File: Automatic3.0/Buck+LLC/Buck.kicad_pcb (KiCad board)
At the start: 2 copper layers, 26 parts, among them J1 OUT, J2 LED, J3 LED, J4 Conn_01x11, J5 LM324, J6 J, J7 Conn_01x01, J8 Conn_01x01, Q1 TIP122, Q2 TIP122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

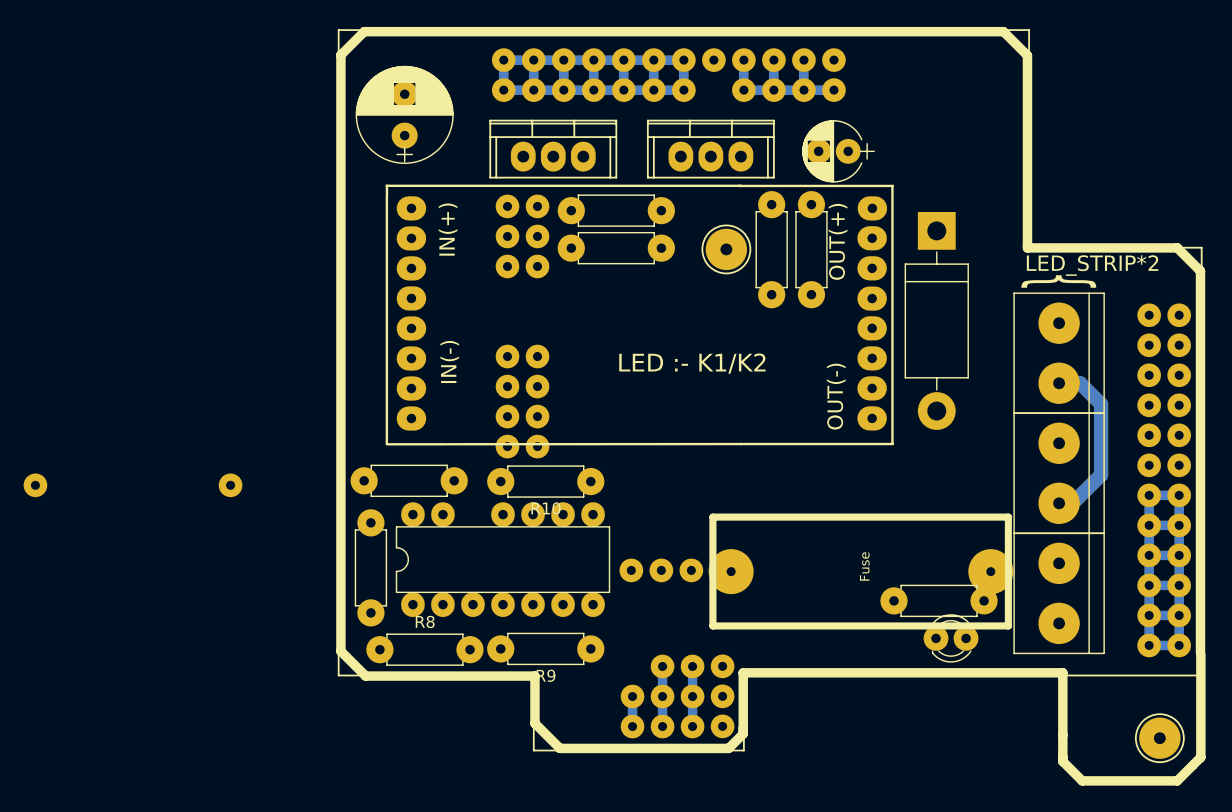
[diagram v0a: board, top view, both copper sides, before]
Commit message: Final automatic base circuits for ABU_ROBOCON_2018 completed
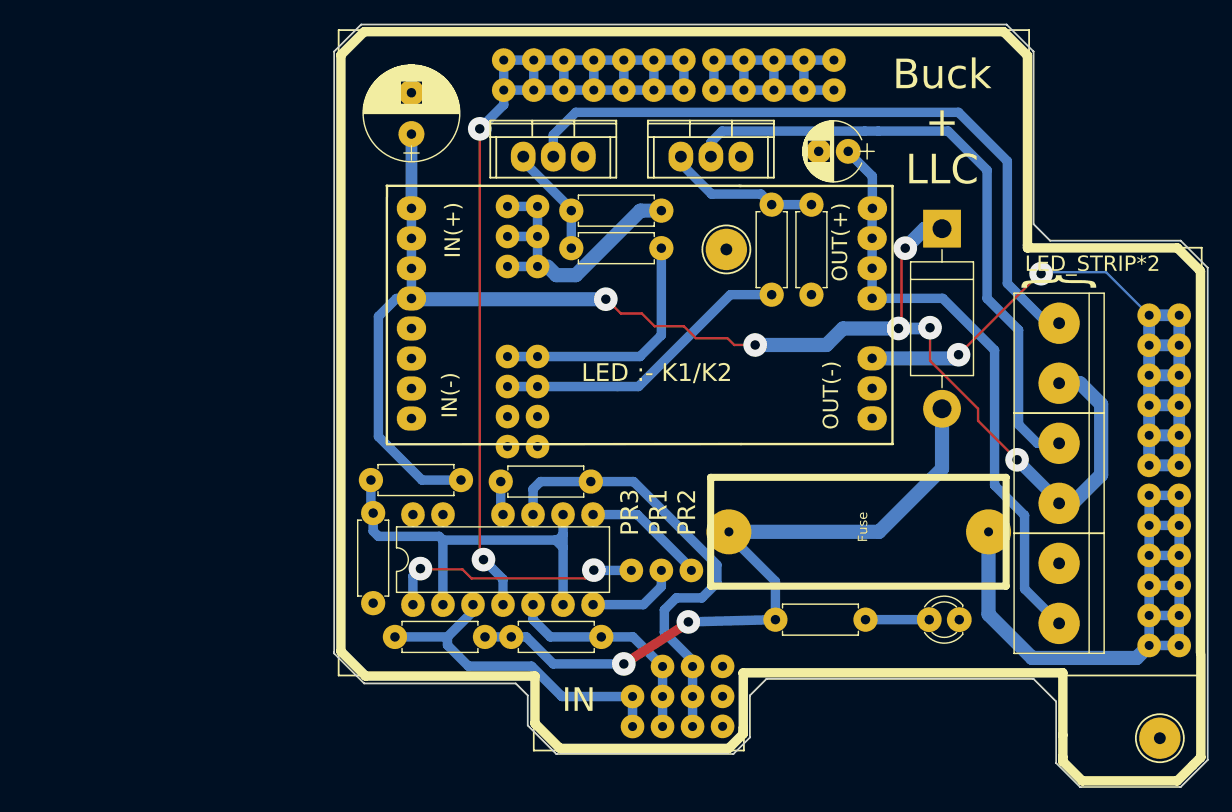
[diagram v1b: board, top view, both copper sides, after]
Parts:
- removed J6: J, modFiles:Jumper
- moved R1 10.2 mm to (214.0, 111.1)
- moved F1 3.37 mm to (213.6, 103.1)
- moved D2 2.53 mm to (221.9, 111.1), turned to 180 degrees
- moved R8 1.67 mm to (174.2, 112.5)
- moved R9 1.35 mm to (191.6, 112.5)
- moved R7 0.85 mm to (172.3, 102.0)
- moved C1 0.59 mm to (175.6, 70.0)
- moved R6 0.58 mm to (172.1, 99.3)
- moved D1 0.48 mm to (220.5, 78.0)
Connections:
- J4 pad 4: /IN1+ -> /IN2+
- J4 pad 5: /IN2+ -> /IN3+
- J4 pad 6: /IN3+ -> /IN1+
- J4 pad 7: /OUT1 -> /OUT2
- J4 pad 8: /OUT2 -> /OUT3
- J4 pad 9: /OUT3 -> /OUT1
- R8 pad 2: +12V -> Net-(D1-Pad2)
- R9 pad 2: +12V -> Net-(D1-Pad2)
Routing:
- net GND: track 15.2 -> 127.7 mm, vias 0 -> 2
- net Net-(C1-Pad1): track 15.9 -> 128.2 mm, vias 0 -> 6
- net Net-(D1-Pad2): track 0.00 -> 61.0 mm, vias 0 -> 2
- net Net-(J2-Pad2): track 0.00 -> 58.9 mm
- net Net-(J3-Pad2): track 0.00 -> 53.1 mm
- net Net-(C2-Pad1): track 0.00 -> 50.8 mm
- net +5V: track 48.3 -> 93.5 mm, vias 0 -> 2
- net /IN3+: track 2.54 -> 38.7 mm
- net /IN1-: track 0.00 -> 35.7 mm
- net /LED2: track 0.00 -> 25.6 mm
- net /IN1+: track 5.08 -> 29.3 mm
- net +12V: track 40.6 -> 63.2 mm
- net /OUT1: track 0.00 -> 21.8 mm, vias 0 -> 2
- net /LED1: track 0.00 -> 21.1 mm
- net /IN2+: track 5.08 -> 19.0 mm
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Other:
- board outline added: 73.9 x 64.5 mm
- net class Default: trace_width 0.25 -> 0.8; via_dia 0.6 -> 2; via_drill 0.4 -> 0.8
- board text added: "Buck + LLC"
- board text added: "IN"
- board text added: "PR3 PR1 PR2"

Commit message: Final for ABU_ROBOCON_2018 Automatic_Base
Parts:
- added J6: LED, modFiles:Connector_Bornier_2, F.Cu at (230.3, 111.4)
- added Q3: TIP122, modFiles:Voltage_Regulators, F.Cu at (224.3, 109.3)
- added R11: 2K2, modFiles:Resistor_small, F.Cu at (216.1, 111.3)
- added R12: 10K, modFiles:Resistor_small, F.Cu at (219.5, 111.3)
- J4: value Conn_01x11 -> Conn_01x12
- moved Q1 38.7 mm to (224.4, 84.0), turned to 90 degrees
- moved J1 36.6 mm to (222.5, 75.6)
- moved Q2 34.3 mm to (224.5, 96.8), turned to 90 degrees
- moved R3 33.6 mm to (219.4, 91.0), turned to 90 degrees
- moved R2 29.3 mm to (216.1, 91.0), turned to 90 degrees
- moved D1 27.9 mm to (192.7, 79.9)
- moved R4 27.1 mm to (216.2, 101.1), turned to 90 degrees
- moved R5 27.1 mm to (219.4, 101.1), turned to 90 degrees
- moved D2 24.0 mm to (200.1, 101.1), turned to 90 degrees
- moved C1 21.1 mm to (176.1, 91.1)
- moved R1 20.1 mm to (200.2, 96.4), turned to 90 degrees
- moved U1 13.6 mm to (175.8, 62.7)
- moved C2 10.1 mm to (220.5, 65.2), turned to 0 degrees
- moved F1 6.75 mm to (207.5, 100.3), turned to 90 degrees
- moved J7 3.09 mm to (200.3, 77.3)
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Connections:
- J1 pad 1: Net-(C2-Pad1) -> GND
- J1 pad 2: GND -> Net-(C2-Pad1)
- J2 pad 1: Net-(C1-Pad1) -> Net-(D1-Pad2)
- J3 pad 1: Net-(C1-Pad1) -> Net-(D1-Pad2)
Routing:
- net Net-(D1-Pad2): track 61.0 -> 128.8 mm
- net Net-(C1-Pad1): track 128.2 -> 65.8 mm, vias 6 -> 0
- net Net-(J2-Pad2): track 58.9 -> 6.84 mm
- net /LED3: track 0.00 -> 51.3 mm, vias 0 -> 2
- net Net-(J3-Pad2): track 53.1 -> 7.19 mm
- net Net-(C2-Pad1): track 50.8 -> 22.1 mm
- net GND: track 127.7 -> 152.2 mm, vias 2 -> 0
- net /LED2: track 25.6 -> 42.2 mm
- net /LED1: track 21.1 -> 34.7 mm
- net +12V: track 63.2 -> 74.4 mm
- net Net-(Q3-Pad1): track 0.00 -> 8.54 mm
- net Net-(J6-Pad2): track 0.00 -> 8.25 mm
- net Net-(Q2-Pad1): track 13.1 -> 9.01 mm
- net Net-(D2-Pad2): track 5.40 -> 2.16 mm
- net /IN3+: track 38.7 -> 36.1 mm
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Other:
- net class Default: clearance 0.2 -> 0.254; trace_width 0.8 -> 0.2
- rule trace_clearance: 0.2 -> 0.254
- board text added: "ANT"
- board text added: "LED:-K1/K2/K3"
- board text added: "P1/P2/P3 :- L4/L6/L2"
- board text added: "POWER"
- board text added: "SAM"
- board text removed: "Buck + LLC"
- board text removed: "LED :- K1/K2"

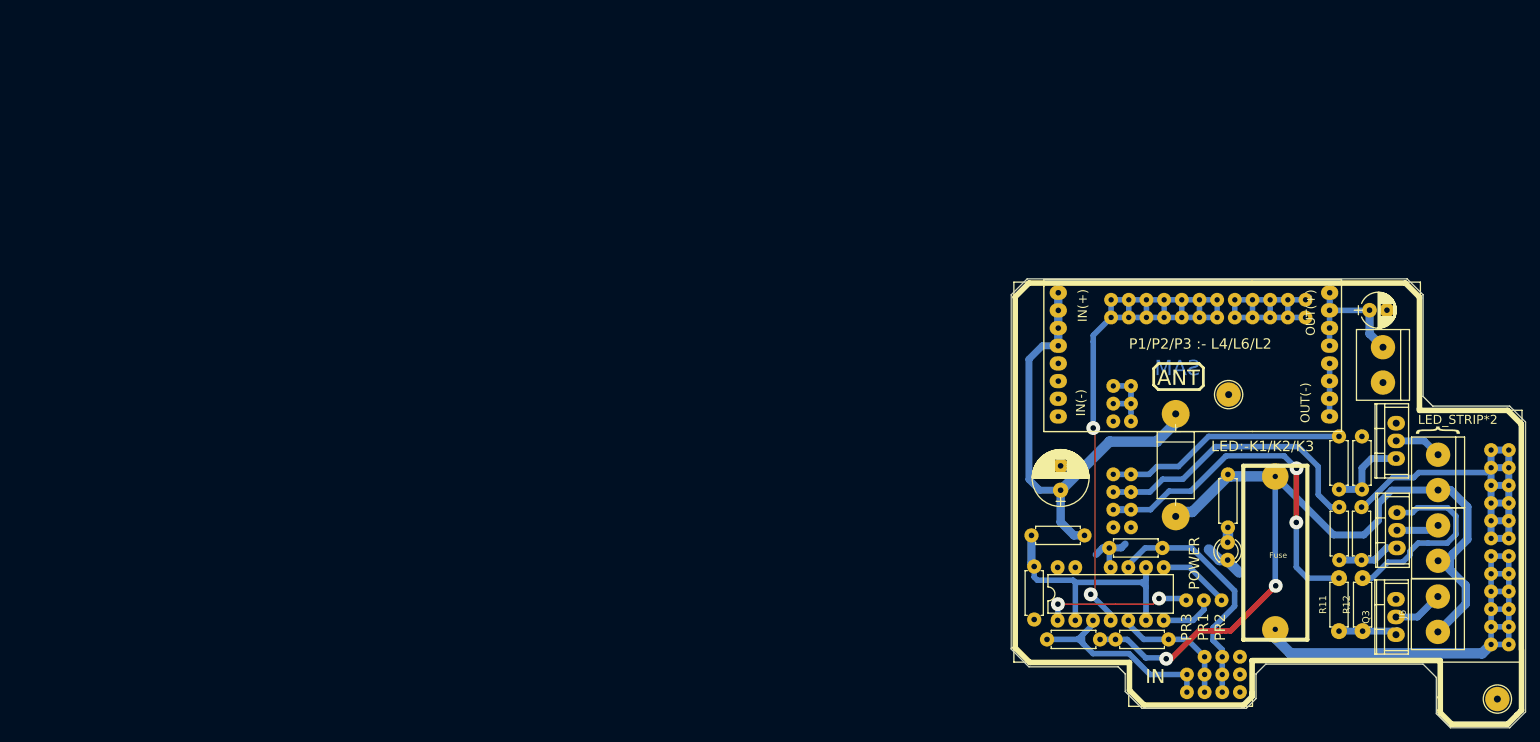
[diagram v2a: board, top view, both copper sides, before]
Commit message: Buck circuit also modified and pdfs also changed
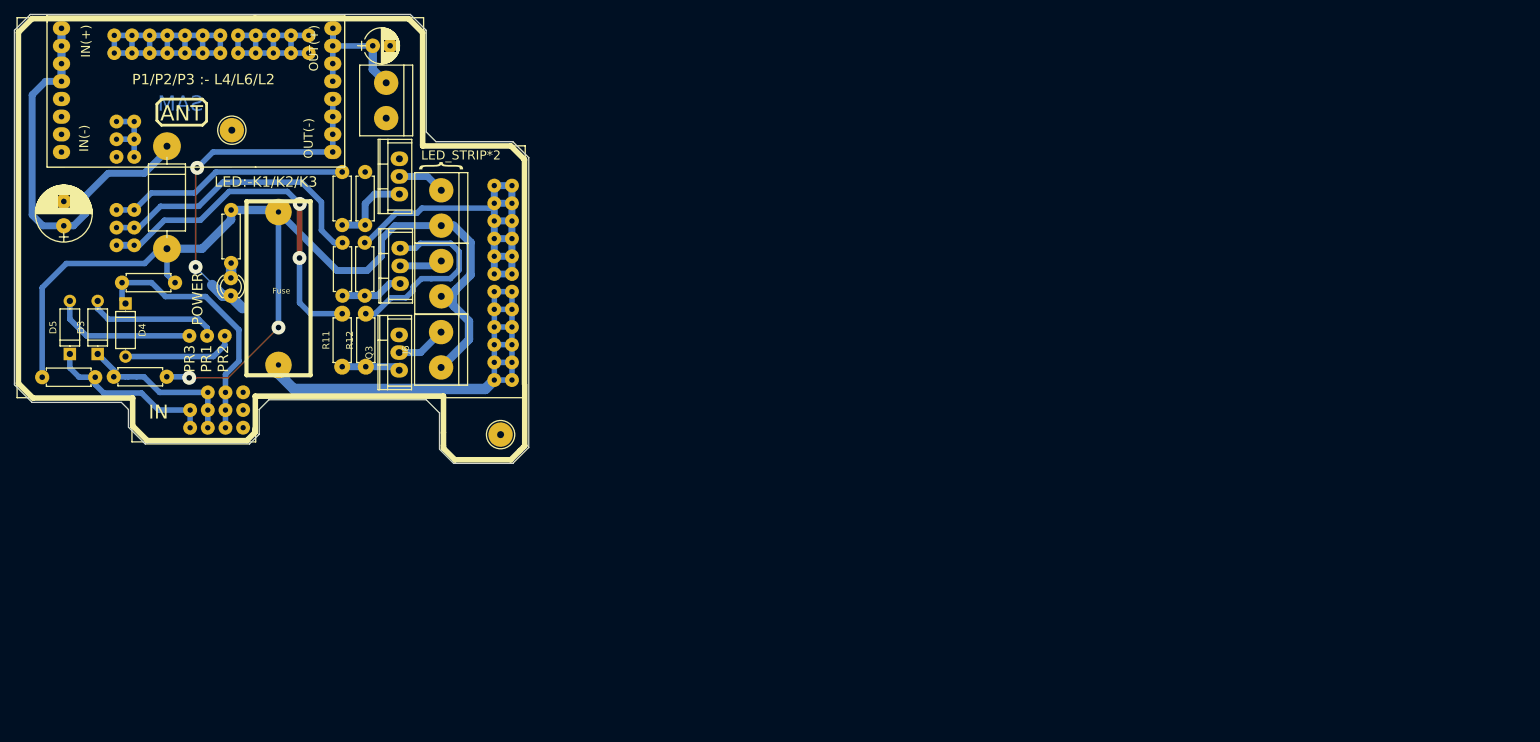
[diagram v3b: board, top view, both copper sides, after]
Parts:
- removed J5: LM324, Housings_DIP:DIP-14_W7.62mm
- removed R6, R7: R, modFiles:Resistor_small
- added D3: D, modFiles:Diode_small, F.Cu at (37.8, 71.5)
- added D4: D, modFiles:Diode_small, F.Cu at (41.8, 64.2)
- added D5: D, modFiles:Diode_small, F.Cu at (33.8, 71.5)
- R10, R8, R9: value 10k -> 39k
- R11, R2, R4: value 2K2 -> 3k3
- moved R9 158.9 mm to (41.2, 61.2), turned to 0 degrees
- moved R10 155.3 mm to (37.4, 74.8)
- moved D1 150.0 mm to (47.7, 41.4)
- moved C1 148.2 mm to (32.9, 53.1)
- moved C2 148.2 mm to (77.3, 27.2)
- moved D2 148.2 mm to (56.9, 63.1)
- moved F1 148.2 mm to (64.2, 62.3)
- moved J1 148.2 mm to (79.2, 37.6)
- moved J2 148.2 mm to (87.1, 53.1)
- moved J3 148.2 mm to (87.1, 63.2)
- moved J4 148.2 mm to (34.4, 29.5)
- moved J6 148.2 mm to (87.1, 73.4)
- moved J7 148.2 mm to (57.0, 39.3)
- moved J8 148.2 mm to (95.7, 83.1)
- moved Q1 148.2 mm to (81.1, 46.0)
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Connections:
- J4 pad 4: /IN2+ -> /PR1
- J4 pad 5: /IN3+ -> /PR2
- J4 pad 6: /IN1+ -> /PR3
- J4 pad 7: /OUT2 -> /PR1o
- J4 pad 8: /OUT3 -> /PR2o
- J4 pad 9: /OUT1 -> /PR3o
- J6 pad 2: Net-(J6-Pad2) -> (no net)
- Q3 pad 2: Net-(J6-Pad2) -> (no net)
- R10 pad 1: /IN3+ -> /PR3
- R10 pad 2: GND -> Net-(D1-Pad2)
- R8 pad 1: /IN1+ -> /PR1
- R9 pad 1: /IN2+ -> /PR2
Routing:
- net +5V: track 94.4 -> 48.9 mm, vias 2 -> 0
- net /PR2: track 0.00 -> 38.2 mm
- net /IN1-: track 37.0 -> 0.00 mm
- net /IN3+: track 36.1 -> 0.00 mm
- net GND: track 152.2 -> 186.1 mm, vias 0 -> 2
- net /IN1+: track 30.5 -> 0.00 mm
- net Net-(D1-Pad2): track 128.8 -> 158.7 mm
- net /PR3: track 0.00 -> 25.2 mm
- net /PR1: track 0.00 -> 23.8 mm
- net /OUT1: track 21.2 -> 0.00 mm, vias 2 -> 0
- net /PR3o: track 0.00 -> 21.2 mm
- net /PR1o: track 0.00 -> 19.1 mm
- net /IN2+: track 18.5 -> 0.00 mm
- net /PR2o: track 0.00 -> 16.7 mm
- net /OUT3: track 10.4 -> 0.00 mm
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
